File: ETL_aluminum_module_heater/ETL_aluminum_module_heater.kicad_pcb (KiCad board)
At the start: 2 copper layers, 48.5 x 58.5 mm, 28 parts, among them J1 Conn_01x01, J2 Conn_01x01

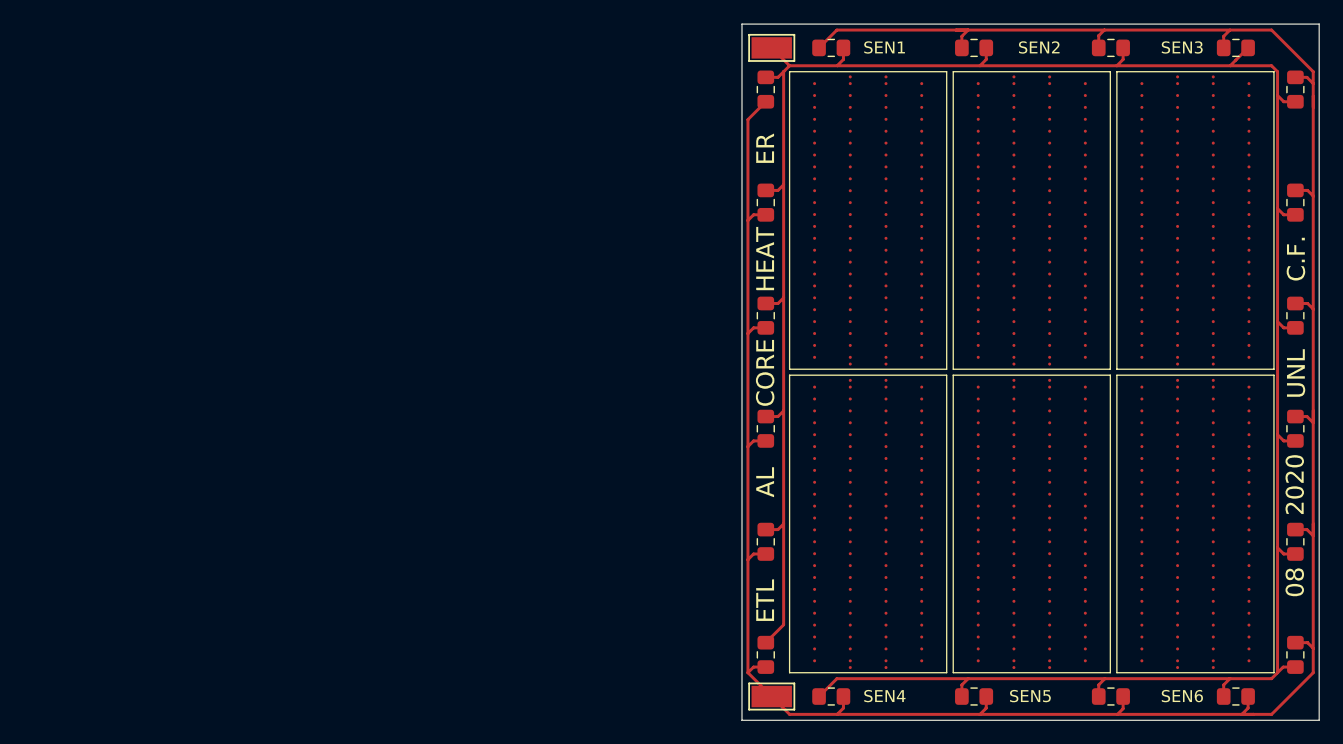
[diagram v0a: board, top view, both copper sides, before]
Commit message: Updates silkscreen on ETL_aluminum_module_heater
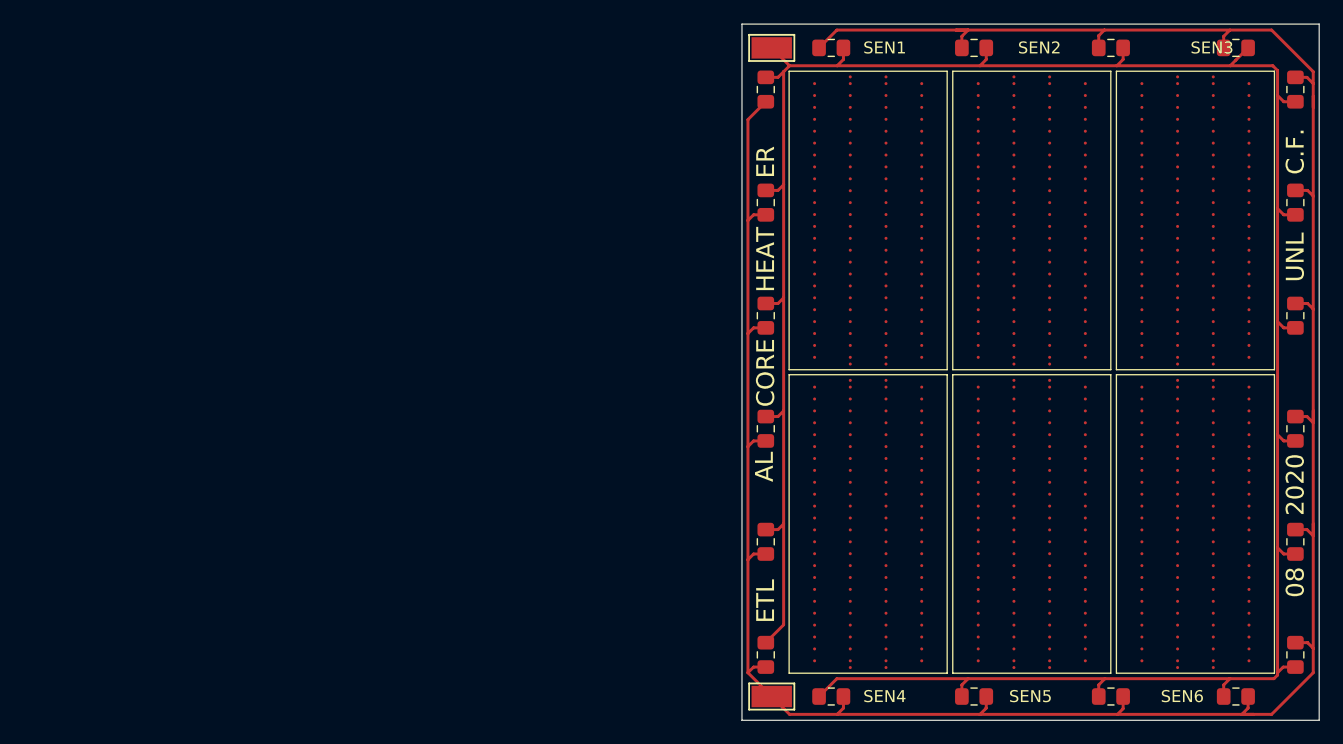
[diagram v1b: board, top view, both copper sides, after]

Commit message: Corrects size of ETL_aluminum_module_heater to 2xsensor size
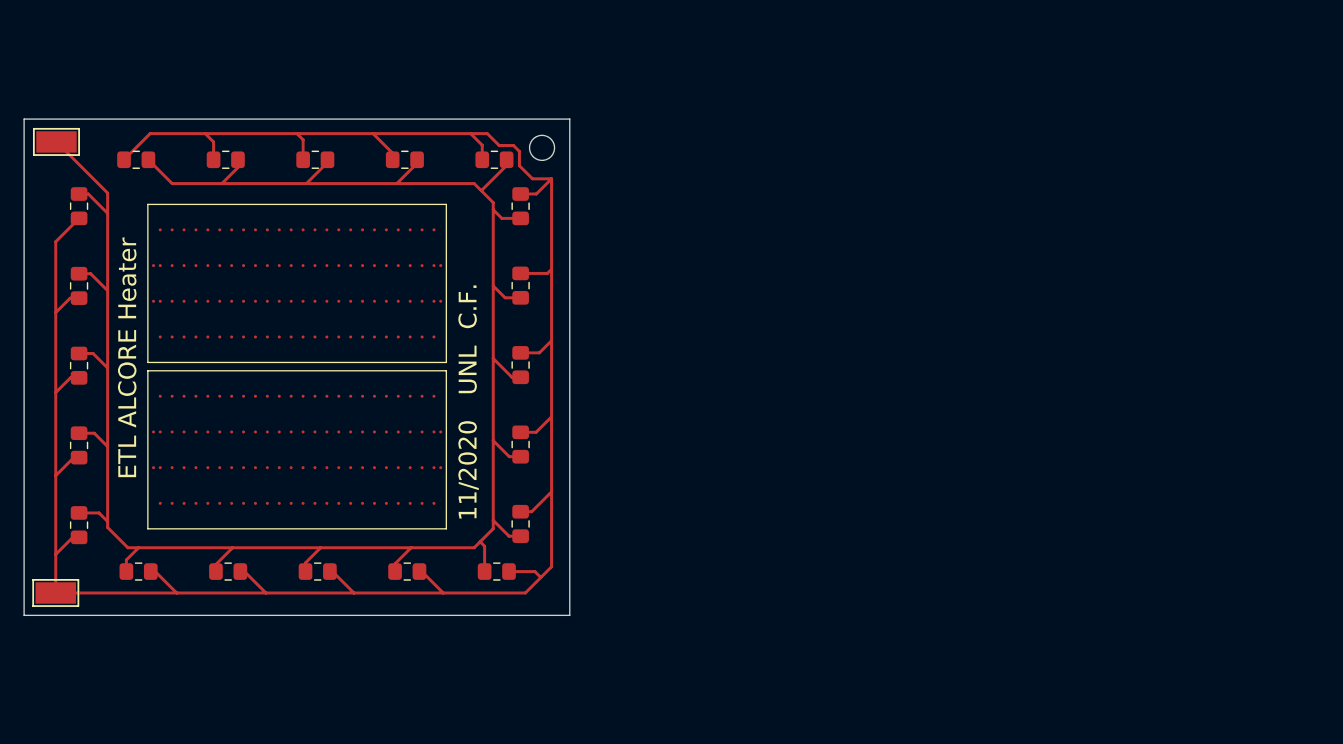
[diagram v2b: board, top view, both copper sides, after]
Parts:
- removed SEN1, SEN3, SEN4, SEN6: ROC1_sans_wirebonds, unl_silab:ROC1_sans_wirebonds
- added REF**: MountingHole_2.1mm, MountingHole:MountingHole_2.1mm, F.Cu at (97.0, 68.4)
- moved SEN2 71.9 mm to (63.9, 86.4), turned to 90 degrees
- moved R20 70.5 mm to (85.4, 69.4)
- moved SEN5 68.8 mm to (63.9, 100.4), turned to 90 degrees
- moved R12 67.6 mm to (93.0, 69.4), turned to 180 degrees
- moved R3 67.5 mm to (77.9, 69.4)
- moved R6 66.0 mm to (95.2, 100.0)
- moved R5 65.6 mm to (95.2, 93.3)
- moved R15 65.3 mm to (95.2, 86.7)
- moved R7 65.1 mm to (95.2, 80.0)
- moved R9 65.1 mm to (95.2, 73.3)
- moved R18 63.6 mm to (70.4, 69.4)
- moved R2 63.5 mm to (70.6, 104.0)
- moved R8 63.0 mm to (93.2, 104.0)
- moved J2 60.8 mm to (56.1, 105.8)
- moved J1 60.6 mm to (56.1, 67.9)
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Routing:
- net /VCC: track 213.9 -> 178.6 mm
- net /GND: track 228.7 -> 196.6 mm
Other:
- board size 48.5 x 58.5 mm -> 45.9 x 41.7 mm
- board text added: "11/2020"
- board text added: "ETL ALCORE Heater"
- board text removed: "08"
- board text removed: "2020"
- board text removed: "AL"
- board text removed: "CORE"
- board text removed: "ER"
- board text removed: "ETL"
- board text removed: "HEAT"
